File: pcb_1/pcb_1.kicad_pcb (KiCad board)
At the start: 2 copper layers, 163.8 x 82.6 mm, 90 parts, among them J1 Screw_Terminal_01x02, J2 Screw_Terminal_01x03, J3 Conn_Relay, J4 Screw_Terminal_01x02, J5 Isolated_ISP, J6 AVR-ISP-6, J7 THERM0, J8 THERM1, K1 DIPxx-1Axx-11x, Q1 BD139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

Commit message: NMOS-symbolit muutettu
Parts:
- removed REF** (x4): MountingHole_4mm, Mounting_Holes:MountingHole_4mm
- Q2, Q3, Q4, Q5, Q6, Q7: value Q_NMOS_DGS -> Q_NMOS_GSD
- moved Q6 36.7 mm to (63.7, 74.8)
- moved Q2 27.9 mm to (82.3, 41.6), turned to 270 degrees
- moved Q4 13.1 mm to (63.5, 54.9), turned to 90 degrees
- moved Q3 6.87 mm to (63.5, 61.5), turned to 90 degrees
- moved Q5 6.17 mm to (63.7, 68.5), turned to 90 degrees
- moved Q7 2.48 mm to (188.4, 94.3), turned to 90 degrees
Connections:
- J5 pad 8: (no net) -> Net-(J5-Pad8)
- Q2 pad 1: Net-(Q2-Pad1) -> SLAVE_MISO
- Q2 pad 2: Net-(J5-Pad4) -> GNDA
- Q2 pad 3: Net-(C17-Pad1) -> Net-(Q2-Pad3)
- Q3 pad 1: Net-(Q3-Pad1) -> Net-(J5-Pad4)
- Q3 pad 2: Net-(J5-Pad5) -> Net-(C17-Pad1)
- Q3 pad 3: Net-(C17-Pad1) -> Net-(Q3-Pad3)
- Q4 pad 1: Net-(Q4-Pad1) -> Net-(J5-Pad5)
- Q4 pad 2: Net-(J5-Pad3) -> Net-(C17-Pad1)
- Q4 pad 3: Net-(C17-Pad1) -> Net-(Q4-Pad3)
- Q5 pad 1: Net-(Q5-Pad1) -> Net-(J5-Pad3)
- Q5 pad 2: Net-(J5-Pad7) -> Net-(C17-Pad1)
- Q5 pad 3: Net-(C17-Pad1) -> Net-(Q5-Pad3)
- Q6 pad 1: Net-(Q6-Pad1) -> Net-(J5-Pad7)
- Q6 pad 2: SLAVE_MISO -> Net-(C17-Pad1)
- Q6 pad 3: GNDA -> Net-(Q6-Pad3)
- Q7 pad 1: Net-(D7-Pad2) -> Net-(J3-Pad2)
- Q7 pad 2: Net-(J3-Pad2) -> Net-(J3-Pad3)
- Q7 pad 3: Net-(J3-Pad3) -> Net-(D7-Pad2)
- R10 pad 2: Net-(Q2-Pad1) -> Net-(Q3-Pad3)
- R11 pad 2: Net-(Q3-Pad1) -> Net-(Q4-Pad3)
- R12 pad 2: Net-(Q4-Pad1) -> Net-(Q5-Pad3)
- R13 pad 2: Net-(Q5-Pad1) -> Net-(Q6-Pad3)
- R18 pad 2: Net-(Q6-Pad1) -> Net-(Q2-Pad3)
- U3 pad 4: (no net) -> Net-(U3-Pad4)
- U6 pad 1: Net-(Q3-Pad1) -> Net-(Q4-Pad3)
- U6 pad 4: Net-(Q2-Pad1) -> Net-(Q3-Pad3)
- U7 pad 1: Net-(Q4-Pad1) -> Net-(Q5-Pad3)
- U7 pad 4: Net-(Q5-Pad1) -> Net-(Q6-Pad3)
- U8 pad 1: (no net) -> Net-(U8-Pad1)
- U8 pad 2: Net-(Q6-Pad1) -> Net-(Q2-Pad3)
- U8 pad 4: (no net) -> Net-(U8-Pad4)
- U9 pad 1: (no net) -> Net-(U9-Pad1)
- U9 pad 10: (no net) -> Net-(U9-Pad10)
- U9 pad 11: (no net) -> Net-(U9-Pad11)
- U9 pad 12: (no net) -> Net-(U9-Pad12)
- U9 pad 13: (no net) -> Net-(U9-Pad13)
- U9 pad 2: (no net) -> Net-(U9-Pad2)
- U9 pad 23: (no net) -> Net-(U9-Pad23)
- U9 pad 30: (no net) -> Net-(U9-Pad30)
- U9 pad 31: (no net) -> Net-(U9-Pad31)
- U9 pad 32: (no net) -> Net-(U9-Pad32)
- U9 pad 7: (no net) -> Net-(U9-Pad7)
- U9 pad 8: (no net) -> Net-(U9-Pad8)
- U9 pad 9: (no net) -> Net-(U9-Pad9)
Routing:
- net Net-(Q5-Pad3): track 0.00 -> 12.6 mm
- net Net-(Q6-Pad3): track 0.00 -> 12.3 mm
- net Net-(Q5-Pad1): track 12.2 -> 0.00 mm
- net Net-(Q2-Pad3): track 0.00 -> 12.1 mm
- net Net-(Q3-Pad3): track 0.00 -> 12.0 mm
- net Net-(Q2-Pad1): track 12.0 -> 0.00 mm
- net Net-(Q4-Pad1): track 11.8 -> 0.00 mm
- net Net-(Q4-Pad3): track 0.00 -> 11.7 mm
- net Net-(Q3-Pad1): track 11.7 -> 0.00 mm
- net Net-(Q6-Pad1): track 9.37 -> 0.00 mm
- net SLAVE_MISO: track 25.7 -> 21.3 mm
- net Net-(J3-Pad2): track 18.2 -> 14.1 mm
- net Net-(J5-Pad7): track 22.8 -> 24.5 mm
- net Net-(J5-Pad3): track 30.8 -> 32.5 mm
- net Net-(D7-Pad2): track 11.2 -> 12.9 mm
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
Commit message: pcb: Silkscreeniä päivitetty
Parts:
- added G***: LOGO, lab_power_supply:Unlimited_power, B.Cu at (117.6, 73.2)
- added REF**: MountingHole_4.3mm_M4, MountingHole:MountingHole_4.3mm_M4, F.Cu at (194.9, 33.7)
- added REF**: MountingHole_4.3mm_M4, MountingHole:MountingHole_4.3mm_M4, F.Cu at (194.9, 107.3)
- added REF**: MountingHole_4.3mm_M4, MountingHole:MountingHole_4.3mm_M4, F.Cu at (40.0, 107.3)
- added REF**: MountingHole_4.3mm_M4, MountingHole:MountingHole_4.3mm_M4, F.Cu at (40.0, 33.7)
- C7: footprint Capacitors_THT:CP_Radial_D8.0mm_P5.00mm -> Capacitor_THT:CP_Radial_D6.3mm_P2.50mm
- moved C22 16.2 mm to (120.8, 53.0), turned to 0 degrees
- moved C6 10.4 mm to (116.6, 58.4), turned to 0 degrees
- moved C7 3.53 mm to (116.5, 64.5), turned to 270 degrees
- moved J8 2.79 mm to (169.9, 39.9), turned to 270 degrees
- moved J7 2.54 mm to (166.1, 35.6), turned to 270 degrees
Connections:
- J7 pad 1: Net-(J7-Pad1) -> GNDA
- J7 pad 2: GNDA -> Net-(J7-Pad2)
- J8 pad 1: Net-(J8-Pad1) -> GNDA
- J8 pad 2: GNDA -> Net-(J8-Pad2)
- R19 pad 2: Net-(J8-Pad1) -> Net-(J8-Pad2)
- R20 pad 2: Net-(J7-Pad1) -> Net-(J7-Pad2)
- U9 pad 26: Net-(J8-Pad1) -> Net-(J8-Pad2)
- U9 pad 27: Net-(J7-Pad1) -> Net-(J7-Pad2)
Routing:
- net Net-(J8-Pad2): track 0.00 -> 53.6 mm
- net Net-(J8-Pad1): track 53.6 -> 0.00 mm
- net Net-(J7-Pad2): track 0.00 -> 53.4 mm
- net Net-(J7-Pad1): track 53.4 -> 0.00 mm
- net +5V: track 299.1 -> 326.8 mm
- net GNDA: vias 6 -> 5

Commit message: pcb: Gerber tiedostot lisätty
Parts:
- added J9: CS, Connector_PinHeader_2.54mm:PinHeader_1x01_P2.54mm_Vertical, F.Cu at (96.5, 52.1)
- added R25: 100, Resistor_SMD:R_0805_2012Metric_Pad1.15x1.40mm_HandSolder, F.Cu at (96.5, 56.4)
- C18, C4: value C -> FB
- C19: value CP -> OUTPUT CAP
- D4: value D_Schottky -> Schottky
- K1: value DIPxx-1Axx-11x -> Relay
- U2: value SPX2920U-5.0 -> 5V REG
- U3: value INA240A1PWR -> INA240
- U4: value MCP4822-E/SN -> MCP4822
- U5: value MCP3422A0-E/SN -> MCP3422
- U6, U7: value HCPL2631SD -> HCPL2631
- U8: value HCPL2601SD -> HCPL2601
- U9: value ATmega328PB-AU -> ATmega328PB
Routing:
- net Net-(J9-Pad1): track 0.00 -> 3.30 mm
- net SLAVE_CS: track 63.3 -> 65.4 mm
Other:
- board text removed: "THERM0"
- board text removed: "THERM1"

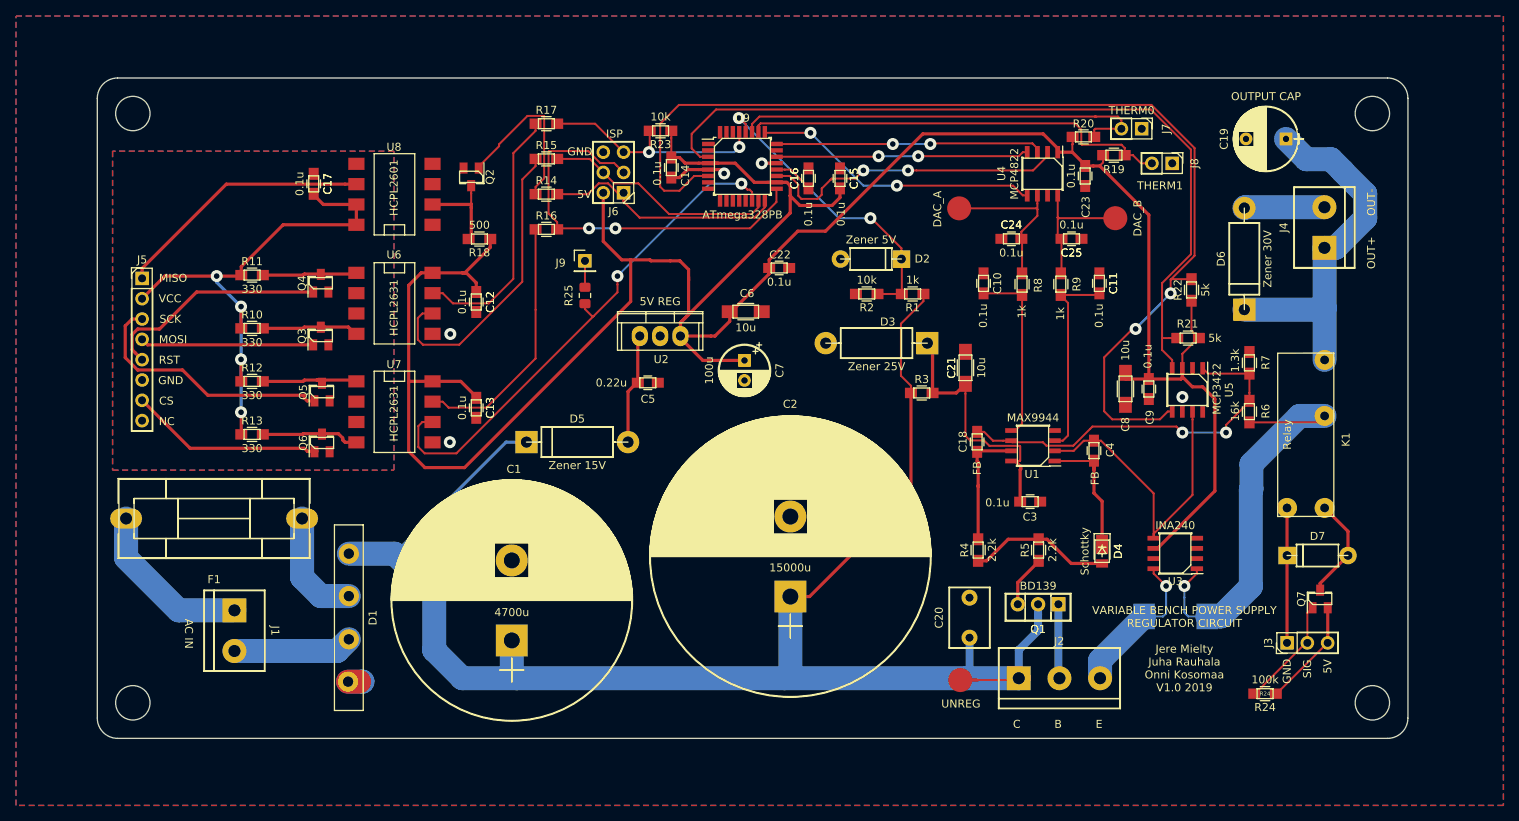
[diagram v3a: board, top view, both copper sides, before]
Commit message: pcb: Kondensaattoreiden footprintit muuttettu
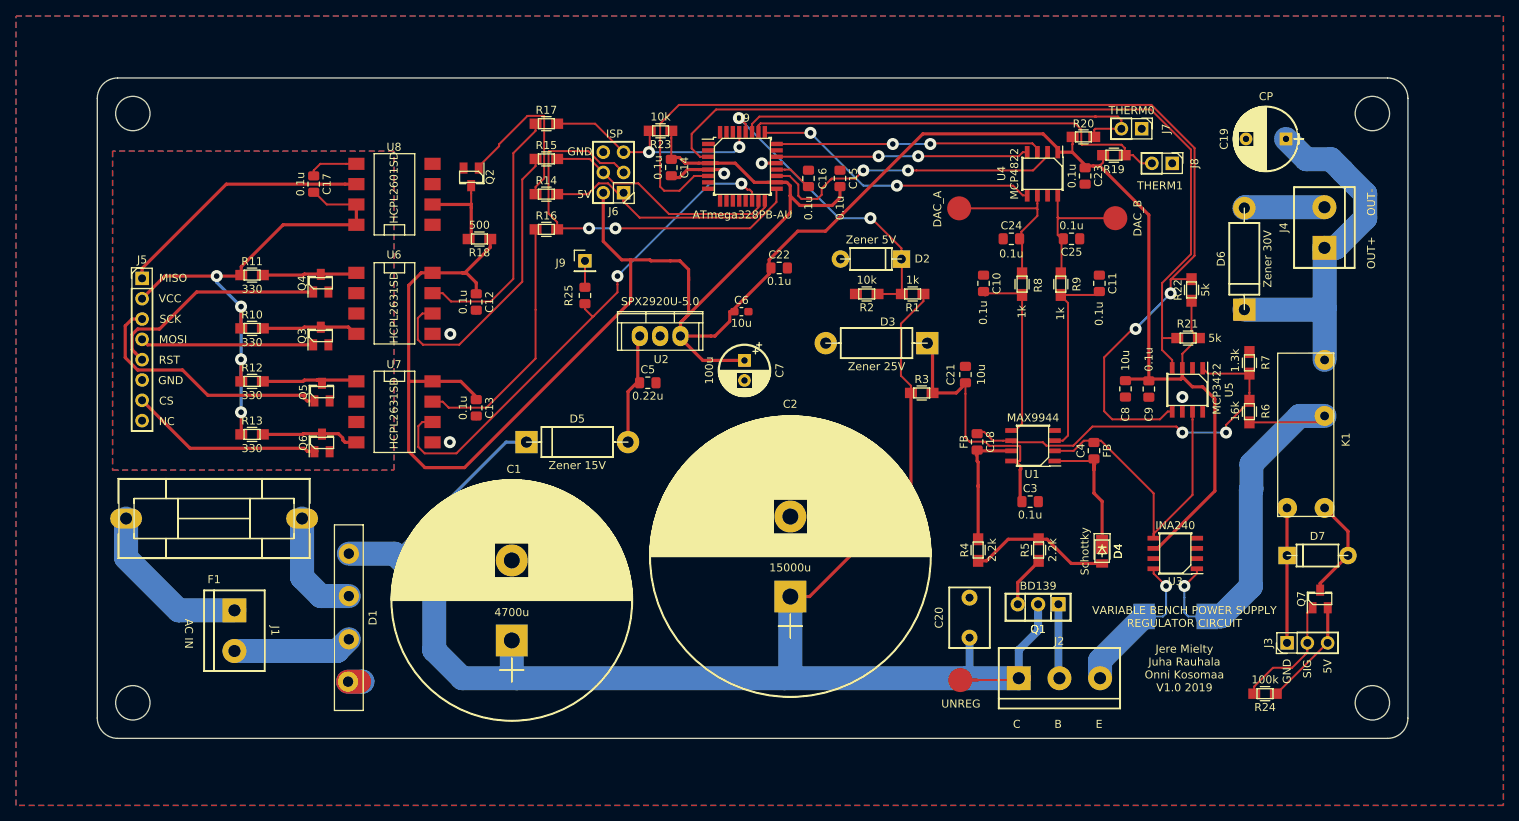
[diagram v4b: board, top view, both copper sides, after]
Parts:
- C10, C11, C12, C13, C14, C15, C16, C17, C18, C22, C23, C24, C25, C3, C4, C5, C9: footprint Capacitors_SMD:C_0805_HandSoldering -> Capacitor_SMD:C_0805_2012Metric_Pad1.15x1.40mm_HandSolder
- C19: value OUTPUT CAP -> CP
- C21, C8: footprint Capacitors_SMD:C_1206_HandSoldering -> Capacitor_SMD:C_0805_2012Metric_Pad1.15x1.40mm_HandSolder
- C6: footprint Capacitors_SMD:C_1206_HandSoldering -> Capacitor_SMD:C_0603_1608Metric_Pad1.05x0.95mm_HandSolder
- K1: value Relay -> DIPxx-1Axx-11x
- U2: value 5V REG -> SPX2920U-5.0
- U6, U7: value HCPL2631 -> HCPL2631SD
- U8: value HCPL2601 -> HCPL2601SD
- U9: value ATmega328PB -> ATmega328PB-AU
- moved C21 0.85 mm to (144.1, 66.3)
- moved C6 0.54 mm to (116.1, 58.4)
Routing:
- net Net-(C17-Pad1): track 0.51 -> 6.86 mm
- net Net-(J3-Pad2): track 14.1 -> 16.7 mm

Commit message: pcb: Optcouplereitten virranrajotinvastkset muutettu
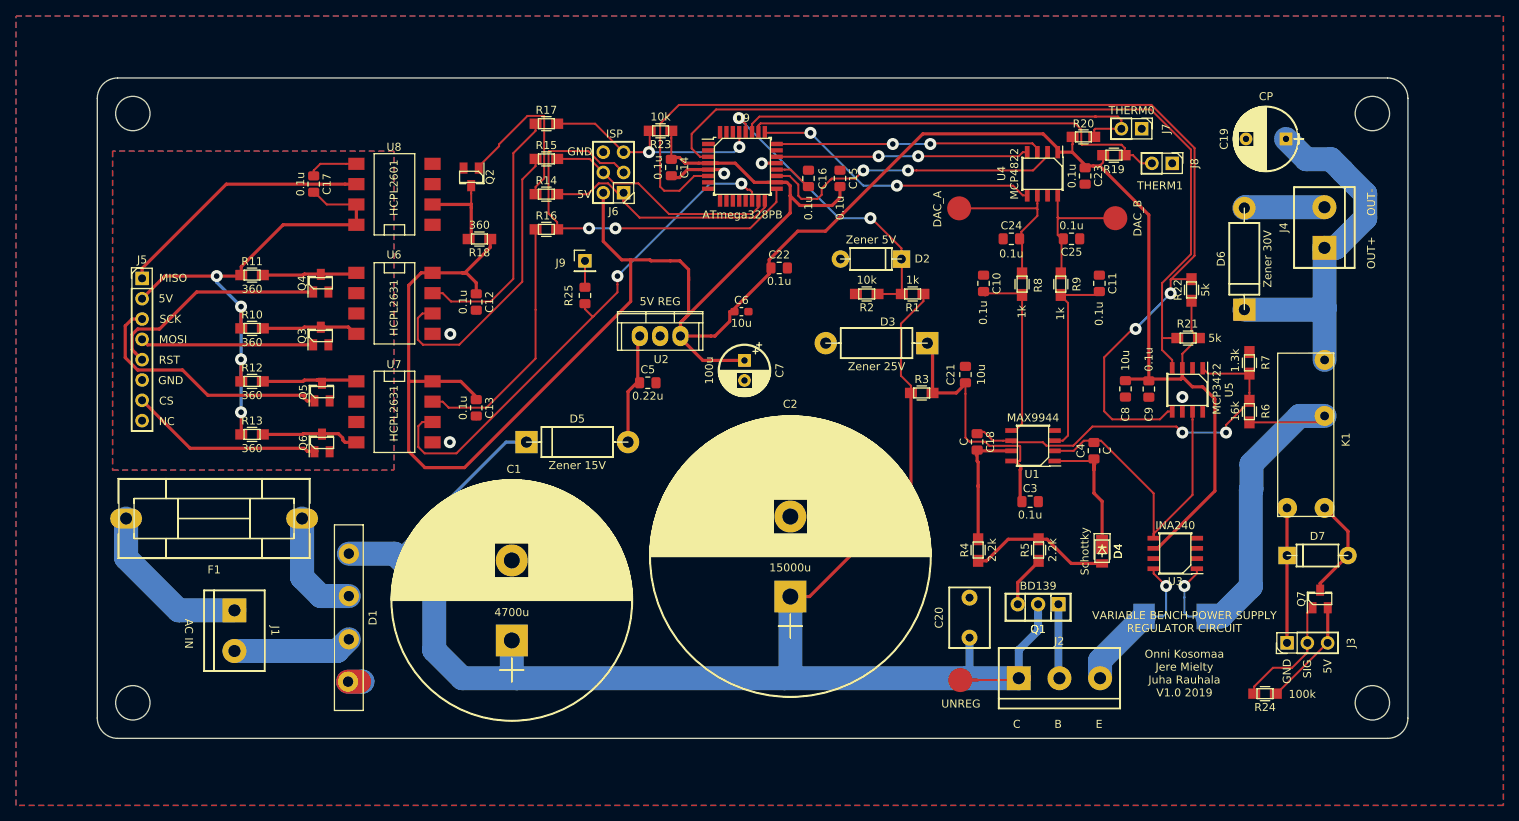
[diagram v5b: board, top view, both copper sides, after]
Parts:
- C18, C4: value FB -> C
- R10, R11, R12, R13: value 330 -> 360
- R18: value 500 -> 360
- U2: value SPX2920U-5.0 -> 5V REG
- U6, U7: value HCPL2631SD -> HCPL2631
- U8: value HCPL2601SD -> HCPL2601
- U9: value ATmega328PB-AU -> ATmega328PB
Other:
- board text added: "VARIABLE BENCH POWER SUPPLY REGULATOR CIRCUIT Onni Kosomaa Jere Mielty Juha Rauhala V1.0 2019"
- board text removed: "VARIABLE BENCH POWER SUPPLY REGULATOR CIRCUIT Jere Mielty Juha Rauhala Onni Kosomaa V1.0 2019"
- board text removed: "VCC"
